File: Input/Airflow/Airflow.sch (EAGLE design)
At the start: 10 parts, among them Q1 MOSFET-NCHANNELBSS123LT1G

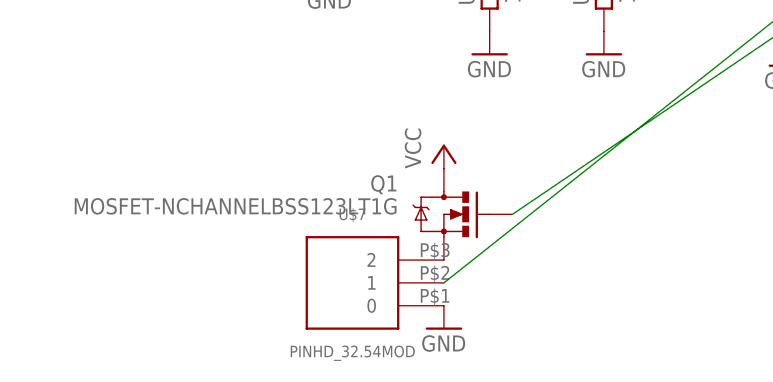
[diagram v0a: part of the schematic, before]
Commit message: Update Pinheader
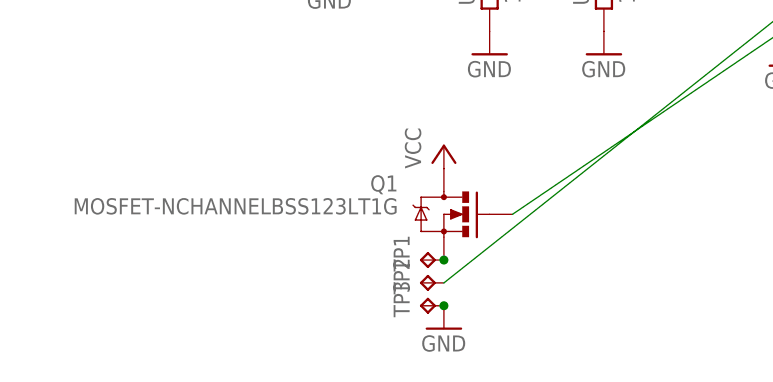
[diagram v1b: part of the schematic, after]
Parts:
- removed U$7: PINHD_32.54MOD, thar:PINHD_32.54MOD
- added TP1, TP2, TP3: TPTP18SQ, testpad:TPTP18SQ
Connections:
- net GND: now also TP3.TP; no longer U$7.0
- net N$6: now also TP2.TP; no longer U$7.1
- net N$7: now also TP1.TP; no longer U$7.2
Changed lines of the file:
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@@
 <setting verticaltext="up"/>
 </settings>
-<grid distance="0.1" unitdist="inch" unit="inch" style="lines" multiple="1" display="no" altdistance="0.01" altunitdist="inch" altunit="inch"/>
+<grid distance="0.05" unitdist="inch" unit="inch" style="lines" multiple="1" display="no" altdistance="0.01" altunitdist="inch" altunit="inch"/>
 <layers>
 <layer number="1" name="Top" color="4" fill="1" visible="yes" active="no"/>
@@
 <part name="P+2" library="supply1" deviceset="VCC" device=""/>
 <part name="P+7" library="supply1" deviceset="VCC" device=""/>
-<part name="U$7" library="thar" deviceset="PINHD_3" device="2.54MOD"/>
 <part name="Q1" library="SparkFun-DiscreteSemi" deviceset="MOSFET-NCHANNEL" device="BSS123LT1G"/>
 <part name="GND8" library="supply1" deviceset="GND" device=""/>
 <part name="P+8" library="supply1" deviceset="VCC" device=""/>
+<part name="TP1" library="testpad" deviceset="TP" device="TP18SQ" value="TPTP18SQ"/>
+<part name="TP2" library="testpad" deviceset="TP" device="TP18SQ" value="TPTP18SQ"/>
+<part name="TP3" library="testpad" deviceset="TP" device="TP18SQ" value="TPTP18SQ"/>
 </parts>
 <sheets>
@@
 <instance part="P+2" gate="VCC" x="38.1" y="123.19"/>
 <instance part="P+7" gate="VCC" x="50.8" y="123.19"/>
-<instance part="U$7" gate="G$1" x="22.86" y="72.39" rot="R180"/>
 <instance part="Q1" gate="G$1" x="33.02" y="80.01" rot="MR0"/>
 <instance part="GND8" gate="1" x="33.02" y="67.31"/>
 <instance part="P+8" gate="VCC" x="33.02" y="87.63"/>
+<instance part="TP1" gate="G$1" x="30.48" y="74.93" rot="R90"/>
+<instance part="TP2" gate="G$1" x="30.48" y="72.39" rot="R90"/>
+<instance part="TP3" gate="G$1" x="30.48" y="69.85" rot="R90"/>
 </instances>
 <busses>
@@
 </segment>
 <segment>
-<pinref part="U$7" gate="G$1" pin="0"/>
 <pinref part="GND8" gate="1" pin="GND"/>
+<pinref part="TP3" gate="G$1" pin="TP"/>
+<junction x="33.02" y="69.85"/>
+<pinref part="TP3" gate="G$1" pin="TP"/>
 </segment>
 </net>
@@
 <net name="N$6" class="0">
 <segment>
-<pinref part="U$7" gate="G$1" pin="1"/>
 <pinref part="U$10" gate="G$1" pin="5"/>
 <wire x1="33.02" y1="72.39" x2="76.2" y2="106.68" width="0.1524" layer="91"/>
+<pinref part="TP2" gate="G$1" pin="TP"/>
 </segment>
 </net>
 <net name="N$7" class="0">
 <segment>
-<pinref part="U$7" gate="G$1" pin="2"/>
 <pinref part="Q1" gate="G$1" pin="S"/>
-</segment>
-</net>
+<pinref part="TP1" gate="G$1" pin="TP"/>
+<junction x="33.02" y="74.93"/>
+<pinref part="TP1" gate="G$1" pin="TP"/>
+</segment>
+</net>
